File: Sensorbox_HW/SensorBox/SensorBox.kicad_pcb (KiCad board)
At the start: 2 copper layers, 84 parts, among them U1 BME280, U11 PS1-O3-100, U12 DS3231M, U13 OPA197xD, U2 OPA197xD, U4 MC33063AD, U5 OPA197xD, U6 MAX31855EASA, U8 HPP845E131R5

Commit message: Layout neue Version fertiggestellt
.
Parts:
- removed the ADC1 at (76.5, 34.7)
- removed the ADC1 at (-30.8, 60.6)
- removed the GND1 at (76.5, 32.1)
- removed the GND1 at (-30.8, 64.7)
- removed the SCL1 at (-30.8, 68.7)
- removed the SCL1 at (76.5, 29.6)
- removed the SDA/Signal1 at (-30.8, 73.2)
- removed the SDA/Signal1 at (76.5, 27.1)
- removed the VCC1 at (-30.8, 76.8)
- removed the VCC1 at (76.5, 24.5)
- added ADC1: Conn_01x01_Socket, Connector_PinHeader_2.00mm:PinHeader_1x01_P2.00mm_Vertical, F.Cu at (109.2, 58.0)
- added GND1: Conn_01x01_Socket, Connector_PinHeader_2.00mm:PinHeader_1x01_P2.00mm_Vertical, F.Cu at (109.2, 54.8)
- added SCL1: Conn_01x01_Socket, Connector_PinHeader_2.00mm:PinHeader_1x01_P2.00mm_Vertical, F.Cu at (109.2, 51.7)
- added SDA/Signal1: Conn_01x01_Socket, Connector_PinHeader_2.00mm:PinHeader_1x01_P2.00mm_Vertical, F.Cu at (109.2, 48.5)
- added VCC1: Conn_01x01_Socket, Connector_PinHeader_2.00mm:PinHeader_1x01_P2.00mm_Vertical, F.Cu at (109.2, 45.3)
- C11, C3, C5, C7, R18, R19, R1_3, R1_4, R1_5, R1_6, Rset1, U2, U5, U6: moved to B.Cu
- C8, CR1220, MicroSD2, R15, R5, U12: moved to F.Cu
- moved R2 174.2 mm to (107.3, 84.4), turned to 90 degrees
- moved R6 168.4 mm to (102.6, 82.0), turned to 180 degrees
- moved R1_2 164.3 mm to (109.2, 90.9), turned to 180 degrees
- moved R10 163.5 mm to (102.4, 88.2)
- moved R1 155.9 mm to (86.8, 92.8)
- moved TP1 154.0 mm to (111.5, 87.5)
- moved U6 150.2 mm to (98.8, 102.3), turned to 180 degrees
- moved C5 149.1 mm to (104.5, 102.2), turned to 90 degrees
- moved R9 149.0 mm to (87.2, 88.4), turned to 90 degrees
- moved JP1 140.6 mm to (112.0, 100.7)
- moved C12 139.7 mm to (102.4, 90.9)
- moved U13 139.4 mm to (94.6, 89.1)
- moved R19 138.9 mm to (77.7, 96.7)
- moved C13 138.7 mm to (102.4, 85.7)
- moved U11 137.6 mm to (99.6, 95.4), turned to 180 degrees
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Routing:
- net VDD_3V3: track 5.35 -> 247.0 mm, vias 0 -> 9
- net VDD_5V: track 0.00 -> 197.7 mm, vias 0 -> 6
- net GND1: track 0.00 -> 187.1 mm, vias 0 -> 59
- net Mosi_GPIO23: track 0.00 -> 87.2 mm, vias 0 -> 2
- net CS_GPIO5: track 0.00 -> 87.1 mm, vias 0 -> 5
- net SCK_GPIO18: track 0.00 -> 83.1 mm, vias 0 -> 2
- net Miso_GPIO19: track 0.00 -> 79.8 mm, vias 0 -> 3
- net RTC_32Khz_GPIO25: track 0.00 -> 72.3 mm, vias 0 -> 1
- net SCK_GPIO14: track 0.00 -> 56.9 mm, vias 0 -> 2
- net Miso_GPIO12: track 0.00 -> 47.4 mm, vias 0 -> 3
- net VDD_2.5V: track 0.00 -> 47.3 mm, vias 0 -> 1
- net Net-(CR1220-+): track 0.00 -> 45.0 mm, vias 0 -> 3
- net RTC_RST_GPIO16: track 0.00 -> 43.6 mm, vias 0 -> 1
- net RTC_INIT_GPIO4: track 0.00 -> 43.2 mm, vias 0 -> 1
- net CS_GPIO15: track 0.00 -> 42.7 mm, vias 0 -> 5
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- added copper zone on B.Cu, net GND1
- added copper zone on F.Cu, net GND1
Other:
- board text removed: "SensorBox V3"

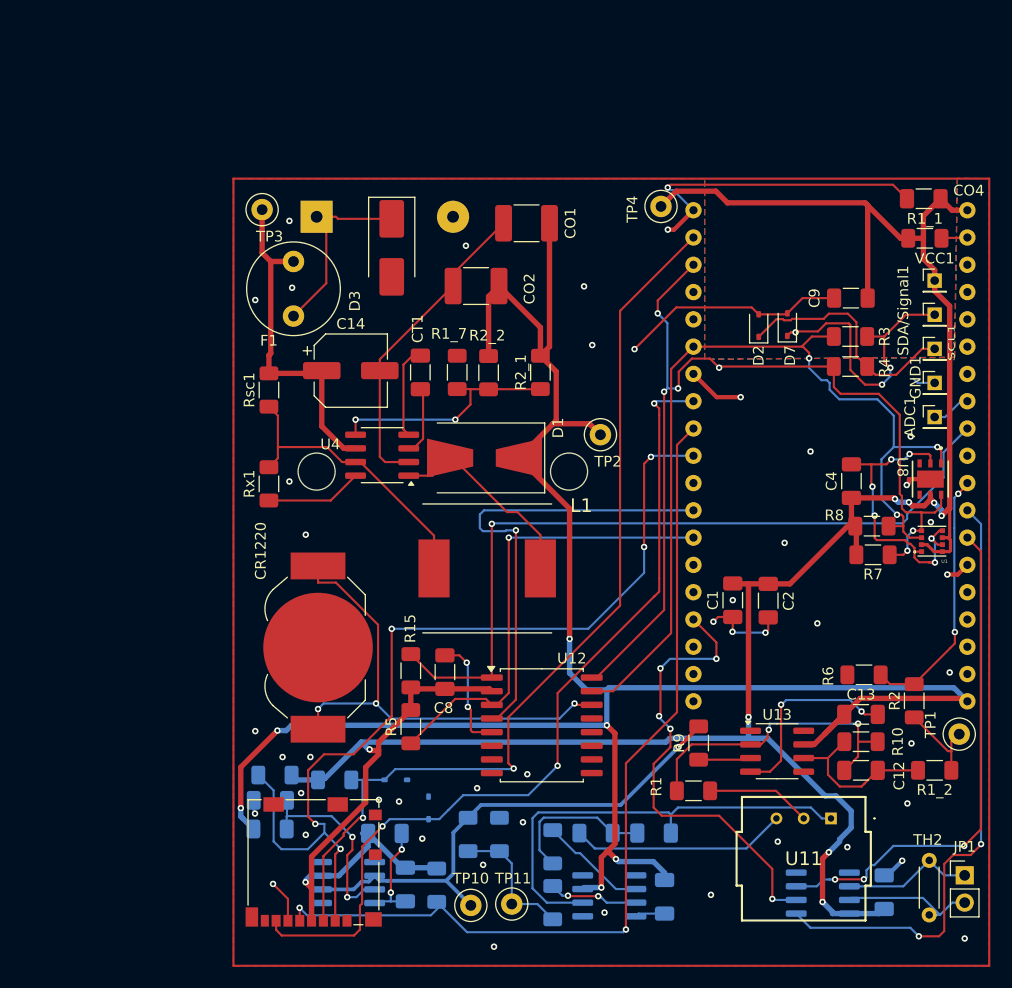
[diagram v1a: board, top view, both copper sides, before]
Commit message: Layout
Layout komplett neugemacht (Sensoren usw. besser platziert.)
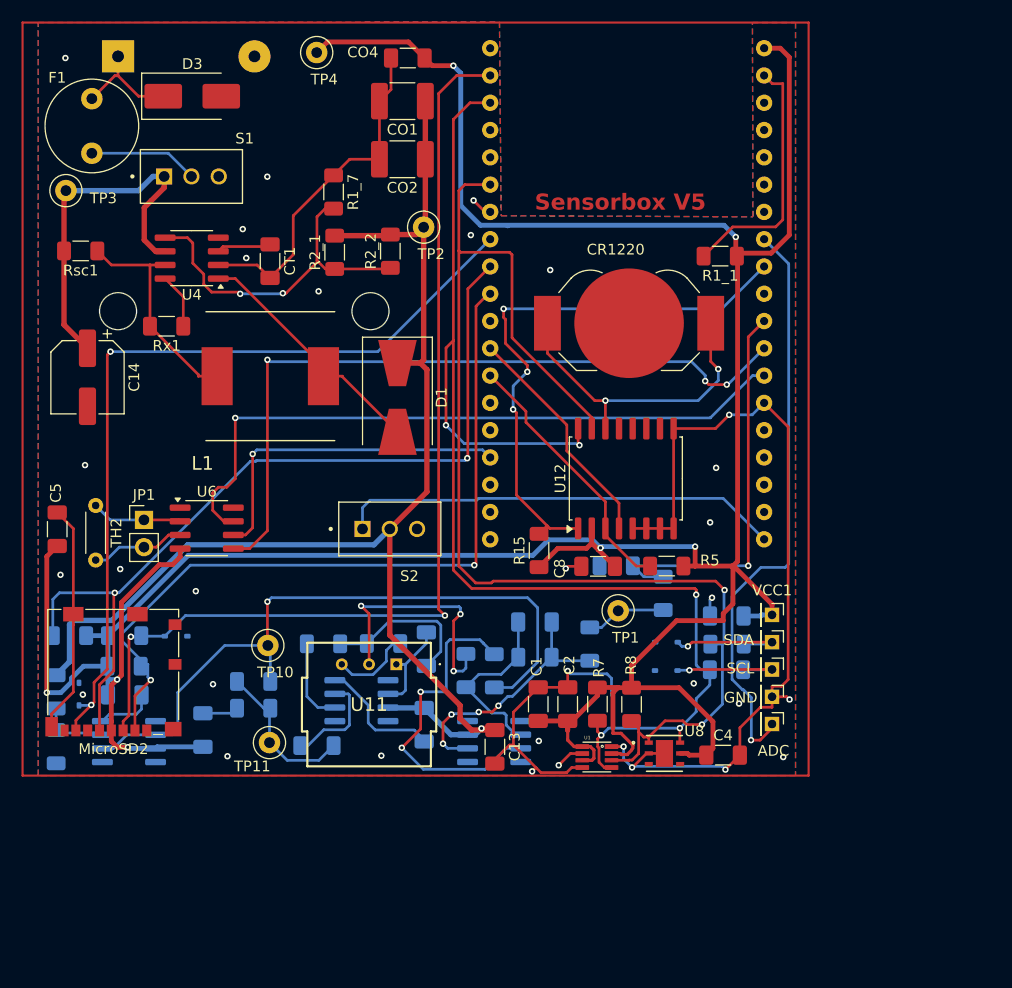
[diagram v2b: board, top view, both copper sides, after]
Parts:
- removed ADC1, GND1, SCL1, SDA/Signal1: Conn_01x01_Socket, Connector_PinHeader_2.00mm:PinHeader_1x01_P2.00mm_Vertical
- added ADC: Conn_01x01_Socket, Connector_PinHeader_2.00mm:PinHeader_1x01_P2.00mm_Vertical, F.Cu at (94.1, 86.6)
- added GND: Conn_01x01_Socket, Connector_PinHeader_2.00mm:PinHeader_1x01_P2.00mm_Vertical, F.Cu at (94.1, 84.0)
- added S1: ATE1D-2M3-10-Z, Schalter_neu:SW_ATE1D-2M3-10-Z, F.Cu at (40.0, 35.6)
- added S2: ATE1D-2M3-10-Z, Schalter_neu:SW_ATE1D-2M3-10-Z, F.Cu at (58.5, 68.4)
- added SCL: Conn_01x01_Socket, Connector_PinHeader_2.00mm:PinHeader_1x01_P2.00mm_Vertical, F.Cu at (94.1, 81.5)
- added SDA: Conn_01x01_Socket, Connector_PinHeader_2.00mm:PinHeader_1x01_P2.00mm_Vertical, F.Cu at (94.1, 79.0)
- C12, C9, D2, D7, R1, R10, R1_2, R2, R3, R4, R6, R9, U13: moved to B.Cu
- C5, U6: moved to F.Cu
- moved TH2 84.3 mm to (31.1, 66.2)
- moved C5 84.1 mm to (27.5, 68.5)
- moved JP1 83.3 mm to (35.6, 67.6)
- moved U6 66.7 mm to (41.5, 68.4), turned to 0 degrees
- moved CO4 49.8 mm to (60.2, 24.6)
- moved U11 42.9 mm to (59.1, 81.0)
- moved CR1220 41.8 mm to (80.8, 49.3), turned to 180 degrees
- moved R33 41.3 mm to (28.7, 78.4), turned to 0 degrees
- moved U1 37.1 mm to (77.8, 89.7), turned to 0 degrees
- moved U8 35.6 mm to (84.1, 89.3), turned to 0 degrees
- moved TP4 35.1 mm to (51.7, 24.1)
- moved VCC1 34.6 mm to (94.1, 76.4), turned to -90 degrees
- moved C13 34.2 mm to (68.3, 88.7), turned to -90 degrees
- moved D4 34.2 mm to (29.6, 83.8)
- moved R1_2 34.2 mm to (77.1, 79.1), turned to -90 degrees
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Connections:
- F1 pad 2: VCC_Bat -> Net-(F1-Pad2)
- U7 pad 19: VDD_5V -> Net-(U7-5V)
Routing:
- net VDD_5V: track 197.7 -> 126.4 mm, vias 6 -> 1
- net VDD_3V3: track 247.0 -> 313.8 mm, vias 9 -> 7
- net extern_Sensor_Gpio_33: track 3.65 -> 54.7 mm, vias 0 -> 1
- net Net-(U7-5V): track 0.00 -> 41.3 mm
- net Net-(C11-Pad1): track 42.3 -> 8.82 mm
- net SDA_GPIO21: track 84.4 -> 116.4 mm, vias 3 -> 2
- net SCL_GPIO22: track 91.3 -> 121.9 mm, vias 6 -> 5
- net Net-(U13-+): track 4.89 -> 30.6 mm, vias 0 -> 2
- net RTC_RST_GPIO16: track 43.6 -> 21.7 mm, vias 1 -> 0
- net Net-(U7-EN): track 2.49 -> 23.5 mm
- net RTC_32Khz_GPIO25: track 72.3 -> 52.9 mm, vias 1 -> 3
- net RTC_INIT_GPIO4: track 43.2 -> 24.7 mm, vias 1 -> 0
- net VDD_2.5V: track 47.3 -> 64.7 mm
- net Miso_GPIO12: track 47.4 -> 63.1 mm, vias 3 -> 1
- net Net-(CR1220-+): track 45.0 -> 29.5 mm, vias 3 -> 2
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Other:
- board text added: "Sensorbox V5"

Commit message: Schalter2-Änderungen
Schalter zwischen 2 GPIOs hinzugefügt
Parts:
- moved S2 6.09 mm to (52.8, 66.2), turned to 0 degrees
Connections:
- S2 pad 1: Net-(U7-5V) -> unconnected-(S2-Pad1)
- S2 pad 2: VDD_5V -> Net-(U7-32)
- S2 pad 3: unconnected-(S2-Pad3) -> Net-(U7-35)
- U7 pad 19: Net-(U7-5V) -> VDD_5V
- U7 pad 6: unconnected-(U7-35-Pad6) -> Net-(U7-35)
- U7 pad 7: unconnected-(U7-32-Pad7) -> Net-(U7-32)
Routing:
- net Net-(U7-35): track 0.00 -> 90.8 mm, vias 0 -> 4
- net Net-(U7-32): track 0.00 -> 68.9 mm, vias 0 -> 1
- net Net-(U7-5V): track 41.3 -> 0.00 mm
- net VDD_5V: track 126.4 -> 160.8 mm, vias 1 -> 3

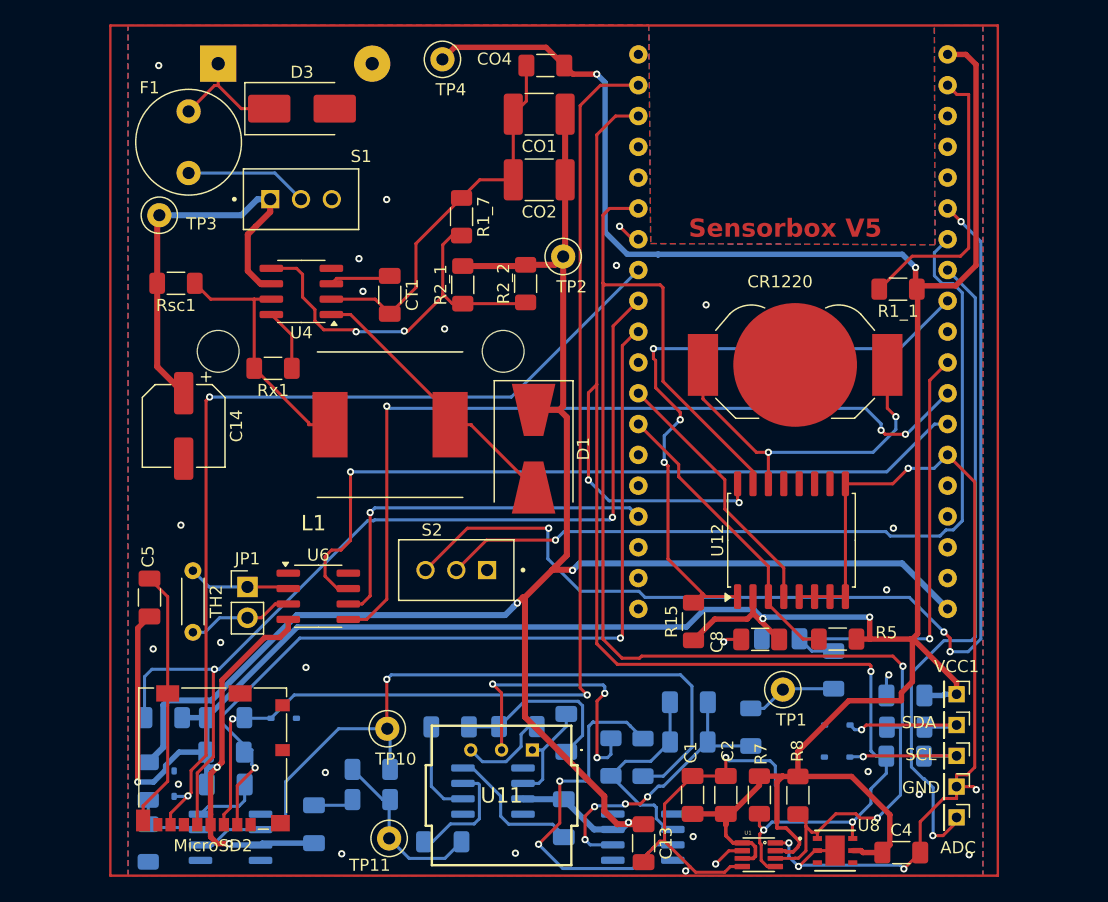
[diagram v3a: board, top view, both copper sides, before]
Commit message: PCB: BME PAD länger designed und Befestigungslöcher hinzugefügt
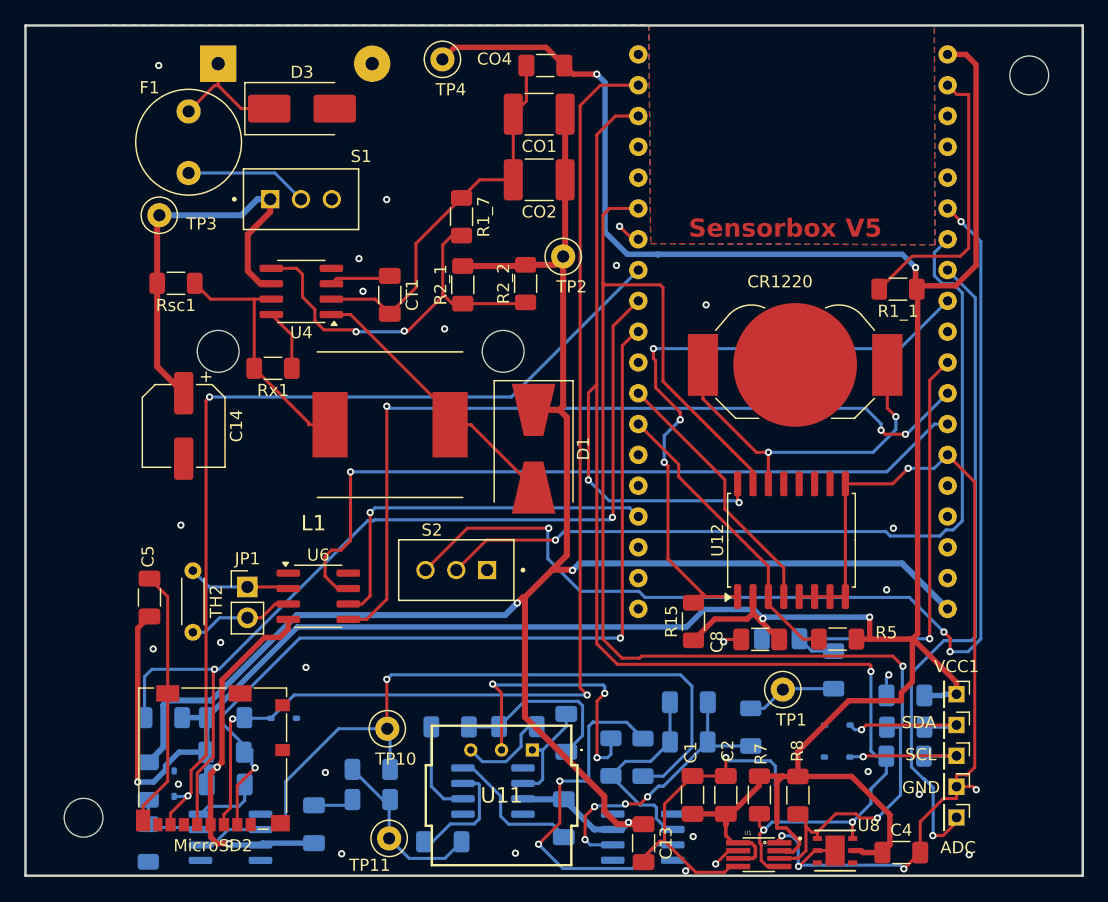
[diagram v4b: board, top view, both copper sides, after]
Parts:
- added REF**: MountingHole_3.2mm_M3, MountingHole:MountingHole_3.2mm_M3, F.Cu at (22.1, 86.6)
- added REF**: MountingHole_3.2mm_M3, MountingHole:MountingHole_3.2mm_M3, F.Cu at (100.1, 25.4)
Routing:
- net GND1: track 190.3 -> 191.3 mm
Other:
- board outline added: 87.2 x 70.1 mm

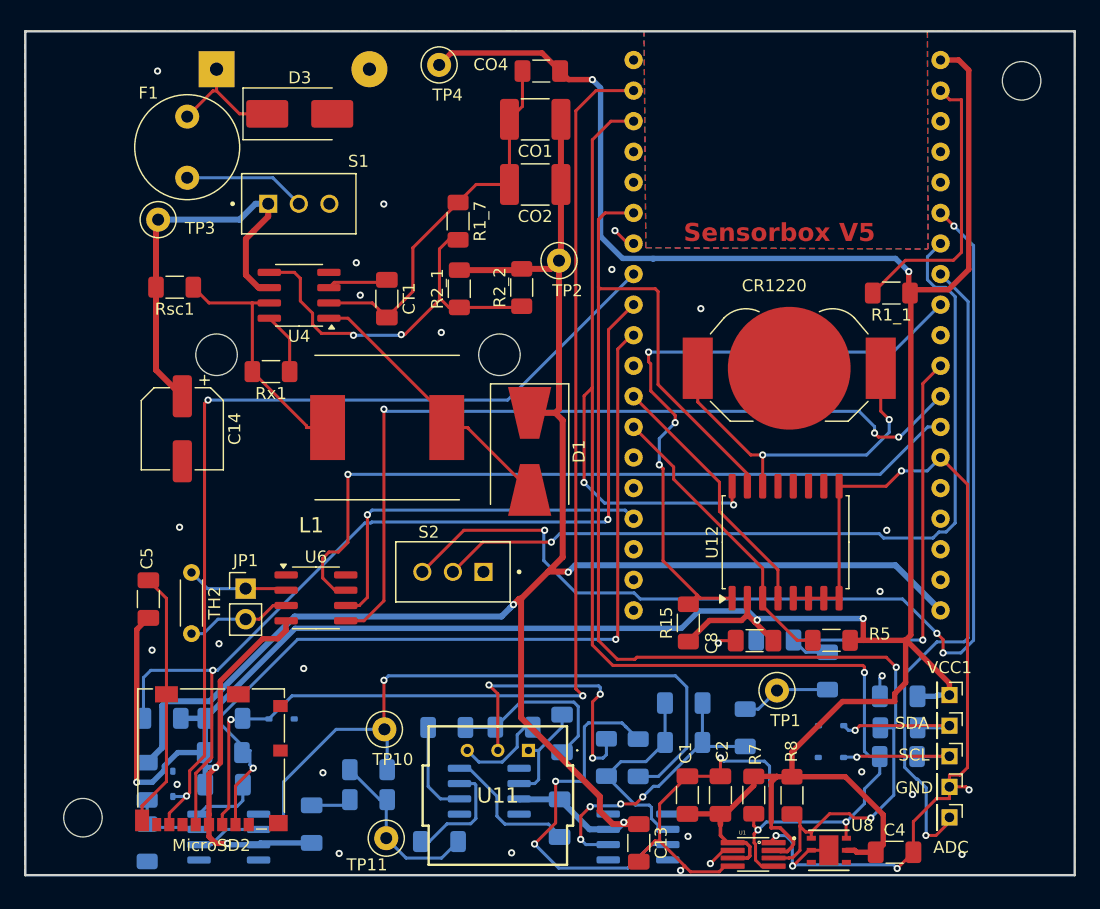
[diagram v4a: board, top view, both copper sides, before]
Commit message: HW-PCB-Change
Die HW wurde angepasst --> Leiterbahnen wurden abgecheckt und geändert; PCB vom BME geändert; GND-Flächen angepasst
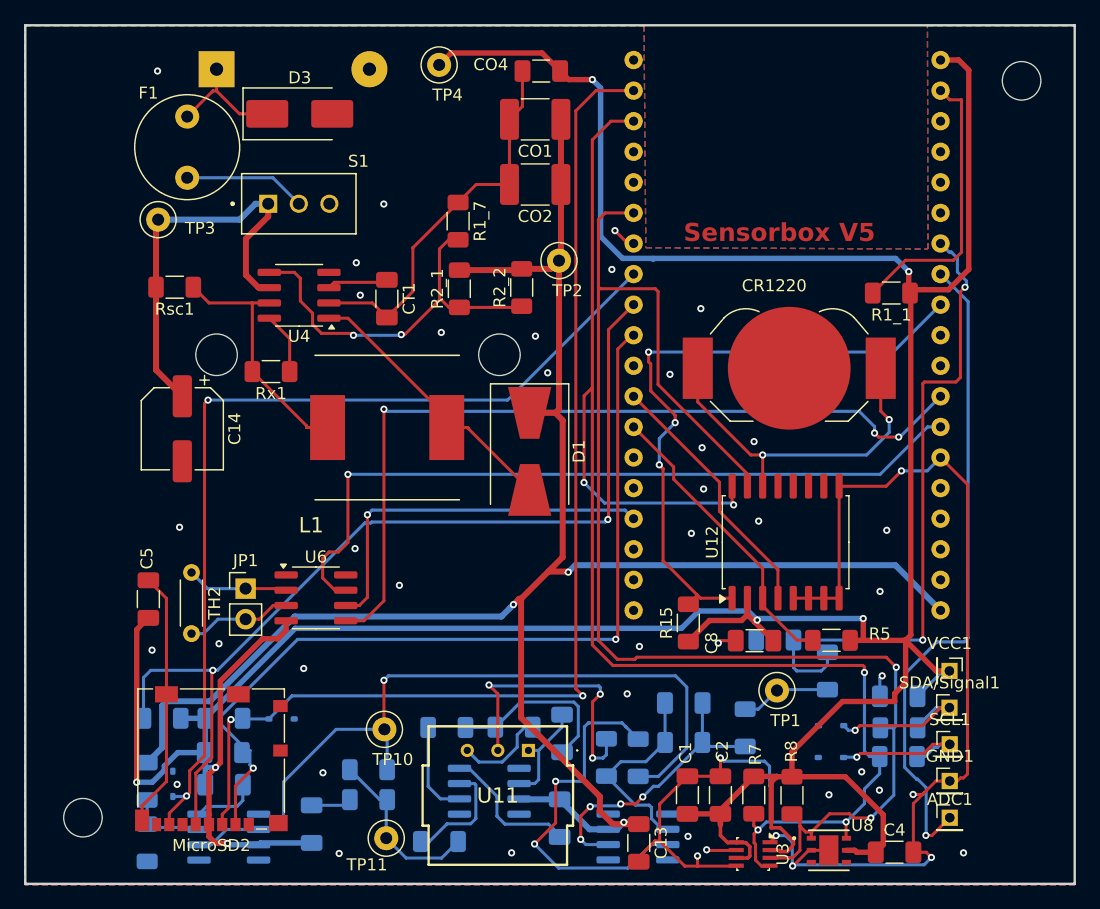
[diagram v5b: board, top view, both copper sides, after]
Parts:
- removed ADC, GND, SCL, SDA: Conn_01x01_Socket, Connector_PinHeader_2.00mm:PinHeader_1x01_P2.00mm_Vertical
- removed S2: ATE1D-2M3-10-Z, Schalter_neu:SW_ATE1D-2M3-10-Z
- removed U1: BME280, BME280 (2):BME280
- added ADC1: Conn_01x01_Socket, Connector_PinHeader_2.00mm:PinHeader_1x01_P2.00mm_Vertical, F.Cu at (94.1, 86.6)
- added GND1: Conn_01x01_Socket, Connector_PinHeader_2.00mm:PinHeader_1x01_P2.00mm_Vertical, F.Cu at (94.1, 83.6)
- added SCL1: Conn_01x01_Socket, Connector_PinHeader_2.00mm:PinHeader_1x01_P2.00mm_Vertical, F.Cu at (94.1, 80.5)
- added SDA/Signal1: Conn_01x01_Socket, Connector_PinHeader_2.00mm:PinHeader_1x01_P2.00mm_Vertical, F.Cu at (94.1, 77.5)
- added U3: BME280, BME_CHANGED:Bosch_LGA-8_2.5x2.5mm_P0.65mm_ClockwisePinNumbering_ch, F.Cu at (77.8, 89.6)
- moved VCC1 2.01 mm to (94.1, 74.4)
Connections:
- R2 pad 2: Ozon_out_ADC_GPIO27 -> Ozon_out_ADC_GPIO32
- R6 pad 1: Ozon_out_ADC_GPIO27 -> Ozon_out_ADC_GPIO32
- U7 pad 11: Ozon_out_ADC_GPIO27 -> unconnected-(U7-27-Pad11)
- U7 pad 6: Net-(U7-35) -> unconnected-(U7-35-Pad6)
- U7 pad 7: Net-(U7-32) -> Ozon_out_ADC_GPIO32
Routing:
- net Net-(U7-35): track 90.8 -> 0.00 mm, vias 4 -> 0
- net Net-(U7-32): track 68.9 -> 0.00 mm, vias 1 -> 0
- net Ozon_out_ADC_GPIO32: track 0.00 -> 53.7 mm, vias 0 -> 2
- net Ozon_out_ADC_GPIO27: track 37.4 -> 0.00 mm, vias 1 -> 0
- net GND1: track 191.3 -> 192.9 mm, vias 32 -> 45
- net Net-(D7-K): track 11.8 -> 13.1 mm
- net Net-(D2-K): track 11.5 -> 12.4 mm
- net VDD_3V3: track 313.8 -> 313.2 mm
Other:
- board size 87.2 x 70.1 mm -> 87.2 x 71.3 mm
